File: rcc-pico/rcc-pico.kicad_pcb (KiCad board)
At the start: 2 copper layers, 78.7 x 59.5 mm, 24 parts, among them J1 PJ-006A, J2 Conn_01x03_Female, SW1 SW_Push, U1 AP63300WU-7, U2 PicoW, U3 Conn_03x20, U4 Conn_03x20

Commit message: finished schematic
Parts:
- removed C5-1, C5-2: 22μ, Capacitor_SMD:C_1210_3225Metric_Pad1.33x2.70mm_HandSolder
- added C1-1: 22μ, Capacitor_SMD:C_1210_3225Metric_Pad1.33x2.70mm_HandSolder, F.Cu at (118.2, 101.3)
- added C1-2: 22μ, Capacitor_SMD:C_1210_3225Metric_Pad1.33x2.70mm_HandSolder, F.Cu at (155.9, 66.0)
- added C5: 4.7u, Capacitor_SMD:C_0603_1608Metric_Pad1.08x0.95mm_HandSolder, F.Cu at (97.1, 110.8)
- added C6: 4.7u, Capacitor_SMD:C_0603_1608Metric_Pad1.08x0.95mm_HandSolder, F.Cu at (101.5, 110.8)
- added J10: Conn_3x3_female, Connector_PinHeader_2.54mm:PinHeader3x3_P2.54mm_Vertical, F.Cu at (155.5, 58.9)
- added J3: Conn_02x03_Top_Bottom, Connector_PinHeader_2.54mm:PinHeader_2x03_P2.54mm_Vertical, F.Cu at (126.9, 77.8)
- added J4: Conn_03x3_female, Connector_PinHeader_2.54mm:PinHeader3x3_P2.54mm_Vertical, F.Cu at (117.1, 98.4)
- added J5: Conn_03x9, 3rdparty:PinHeader_3x9_P2.54mm_Vertical, F.Cu at (116.8, 73.4)
- added J6: Conn_03x3_female, Connector_PinHeader_2.54mm:PinHeader3x3_P2.54mm_Vertical, F.Cu at (138.9, 85.4)
- added J7: Conn_02x03_Top_Bottom, Connector_PinHeader_2.54mm:PinHeader_2x03_P2.54mm_Vertical, F.Cu at (148.0, 64.2)
- added J8: Conn_04x4, Connector_PinHeader_2.54mm:PinHeader4x4_P_2.54mm_Vertical, F.Cu at (128.0, 74.7)
- added J9: Conn_02x02_Top_Bottom, Connector_PinHeader_2.54mm:PinHeader_2x02_P2.54mm_Vertical, F.Cu at (170.1, 50.4)
- added Q1: BSS138, Package_TO_SOT_SMD:SOT-23, F.Cu at (153.0, 73.8)
- added Q2: BSS138, Package_TO_SOT_SMD:SOT-23, F.Cu at (130.6, 95.6)
- added Q3: BSS138, Package_TO_SOT_SMD:SOT-23, F.Cu at (148.1, 73.8)
- added R4: 10K, Resistor_SMD:R_0402_1005Metric, F.Cu at (122.7, 100.1)
- added R5: 500, Resistor_SMD:R_0603_1608Metric, F.Cu at (154.9, 69.4)
- added R6: 10K, Resistor_SMD:R_0402_1005Metric, F.Cu at (113.7, 100.1)
- added R7: 10K, Resistor_SMD:R_0402_1005Metric, F.Cu at (123.6, 97.6)
- added R8: 10K, Resistor_SMD:R_0402_1005Metric, F.Cu at (126.5, 97.6)
- added R9: 10K, Resistor_SMD:R_0402_1005Metric, F.Cu at (169.0, 56.3)
- added SW-on/off2: SW_SPST, 3rdparty:SW-T2-4E-B-A2-MA2, F.Cu at (124.5, 52.6)
- C3: value 100n -> 0.1μ
- J2: value Conn_01x03_Female -> Screw_Terminal; footprint Connector_PinHeader_2.54mm:PinHeader_1x03_P2.54mm_Vertical -> TerminalBlock_Phoenix:TerminalBlock_Phoenix_MPT-0,5-2-2.54_1x02_P2.54mm_Horizontal
- L1: value 6.8u -> 4.7u; footprint Inductor_SMD:L_Wuerth_HCI-1365 -> Inductor_SMD:SIDMP-SP0530
- R3: value 500 -> 10K; footprint Resistor_SMD:R_0603_1608Metric -> Resistor_SMD:R_0402_1005Metric
- U4: value Conn_03x20 -> AP2115M-3.3TRG1; footprint 3rdparty:PinHeader_3x20_P2.54mm_Vertical -> Package_SO:AP2115M-3.3TRG1
- moved J2 92.3 mm to (82.3, 107.1)
- moved D1 87.3 mm to (105.7, 110.8), turned to 0 degrees
- moved C3 85.7 mm to (92.0, 110.6), turned to 0 degrees
- moved H3 84.5 mm to (111.6, 104.8)
- moved R2 80.6 mm to (110.8, 110.1), turned to 0 degrees
- moved C4 78.1 mm to (115.7, 109.7)
- moved R3 77.4 mm to (116.7, 104.4), turned to 0 degrees
- moved L1 70.5 mm to (103.4, 105.3)
- moved SW1 68.6 mm to (90.7, 102.8), turned to 0 degrees
- moved C1 68.1 mm to (125.2, 94.5), turned to 0 degrees
- moved J1 53.9 mm to (119.5, 78.1), turned to 0 degrees
- moved H1 43.2 mm to (164.2, 51.7)
- moved H2 38.3 mm to (135.4, 89.8)
- moved TP1 32.6 mm to (161.2, 62.1)
- moved SW-on/off1 31.9 mm to (138.8, 52.6)
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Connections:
- D1 pad 2: +5V -> +3.3V
- H1 pad 1: unconnected-(H1-Pad1) -> GND
- H2 pad 1: unconnected-(H2-Pad1) -> GND
- H3 pad 1: unconnected-(H3-Pad1) -> GND
- H4 pad 1: unconnected-(H4-Pad1) -> GND
- J2 pad 1: +9V -> /MTRPWR
- R3 pad 1: Net-(D1-Pad1) -> +5V
- R3 pad 2: GND -> /5V_PWM_1
- U2 pad 33: /AGND -> GND
- U2 pad 35: /ADC_VREF -> unconnected-(U2-Pad35)
- U2 pad 36: /3V3 -> unconnected-(U2-Pad36)
- U2 pad 37: /3V3_EN -> unconnected-(U2-Pad37)
- U2 pad 40: /VBUS -> unconnected-(U2-Pad40)
- U3 pad 1: GND -> /GPIO0
- U3 pad 10: GND -> /GPIO7
- U3 pad 11: GND -> /GPIO8
- U3 pad 12: GND -> /GPIO9
- U3 pad 14: GND -> /GPIO10
- U3 pad 15: GND -> /GPIO11
- U3 pad 16: GND -> /GPIO12
- U3 pad 17: GND -> /GPIO13
- U3 pad 19: GND -> /GPIO14
- U3 pad 2: GND -> /GPIO1
- U3 pad 20: GND -> /GPIO15
- U3 pad 21: +5V -> +3.3V
- U3 pad 22: +5V -> +3.3V
- U3 pad 23: +5V -> +3.3V
- U3 pad 24: +5V -> +3.3V
- U3 pad 25: +5V -> +3.3V
- U3 pad 26: +5V -> +3.3V
- U3 pad 27: +5V -> +3.3V
- U3 pad 28: +5V -> +3.3V
- U3 pad 29: +5V -> +3.3V
- U3 pad 30: +5V -> +3.3V
- U3 pad 31: +5V -> +3.3V
- U3 pad 32: +5V -> +3.3V
- U3 pad 33: +5V -> +3.3V
- U3 pad 34: +5V -> +3.3V
- U3 pad 35: +5V -> +3.3V
- U3 pad 36: +5V -> +3.3V
- U3 pad 37: +5V -> +3.3V
- U3 pad 38: +5V -> +3.3V
- U3 pad 39: +5V -> +3.3V
- U3 pad 4: GND -> /GPIO2
- U3 pad 40: +5V -> +3.3V
- U3 pad 41: /GPIO0 -> GND
- U3 pad 42: /GPIO1 -> GND
- U3 pad 44: /GPIO2 -> GND
- U3 pad 45: /GPIO3 -> GND
- U3 pad 46: /GPIO4 -> GND
- U3 pad 47: /GPIO5 -> GND
- U3 pad 49: /GPIO6 -> GND
- U3 pad 5: GND -> /GPIO3
- U3 pad 50: /GPIO7 -> GND
- U3 pad 51: /GPIO8 -> GND
- U3 pad 52: /GPIO9 -> GND
- U3 pad 54: /GPIO10 -> GND
- U3 pad 55: /GPIO11 -> GND
- U3 pad 56: /GPIO12 -> GND
- U3 pad 57: /GPIO13 -> GND
- U3 pad 59: /GPIO14 -> GND
- U3 pad 6: GND -> /GPIO4
- U3 pad 60: /GPIO15 -> GND
- U3 pad 7: GND -> /GPIO5
- U3 pad 9: GND -> /GPIO6
- U4 pad 1: /VBUS -> +3.3V
- U4 pad 2: +5V -> unconnected-(U4-Pad2)
- U4 pad 3: GND -> unconnected-(U4-Pad3)
- U4 pad 4: /3V3_EN -> unconnected-(U4-Pad4)
- U4 pad 5: /3V3 -> +5V
- U4 pad 6: /ADC_VREF -> GND
- U4 pad 7: /GPIO28 -> GND
- U4 pad 8: /AGND -> +5V
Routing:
- net +5V: track 227.8 -> 0.00 mm, vias 1 -> 0
- net +9V: track 45.0 -> 0.00 mm, vias 2 -> 0
- net /run: track 24.1 -> 0.00 mm
- net Net-(C3-Pad2): track 19.3 -> 0.00 mm
- net Net-(J1-Pad1): track 16.9 -> 0.00 mm
- net Net-(C4-Pad1): track 11.9 -> 0.00 mm
- net /GPIO18: track 7.29 -> 0.00 mm
- net /GPIO22: track 7.29 -> 0.00 mm
- net /ADC_VREF: track 7.29 -> 0.00 mm
- net /3V3_EN: track 7.29 -> 0.00 mm
- net /3V3: track 7.29 -> 0.00 mm
- net /VBUS: track 7.29 -> 0.00 mm
- net /GPIO28: track 7.29 -> 0.00 mm
- net /GPIO27: track 7.29 -> 0.00 mm
- net /GPIO26: track 7.29 -> 0.00 mm
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- removed copper zone on F.Cu, net GND
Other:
- board outline removed
- board text removed: "+5V"
- board text removed: "+9V BATTERY"
- board text removed: "+9V GND +5V"
- board text removed: "0 1"
- board text removed: "10 11 12 13"
- board text removed: "14 15"
- board text removed: "17 16"
- board text removed: "2 3 4 5"
- board text removed: "21 20 19 18"
- board text removed: "22"
- board text removed: "27 26"
- board text removed: "28"
- board text removed: "3V3 ADC_VREF"
- board text removed: "3V3_EN"
- board text removed: "6 7 8 9"
- board text removed: "AGND"
- board text removed: "GND"
- board text removed: "Jeannette Circe & Michael Giglia"
- board text removed: "L298N"
- board text removed: "ON OFF OFF"
- board text removed: "PICO"
- board text removed: "PICO RESET"
- board text removed: "Power Switch"
- board text removed: "ROBOTICS CRASH COURSE '23 RP PICO SHIELD v0.1"
- board text removed: "SUMMER STEM"
- board text removed: "THE COOPER UNION"
- board text removed: "USB"
- board text removed: "VBUS +5V GND"
- board text removed: "run"

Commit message: finished schematic and layout
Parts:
- removed C1-1, C1-2: 22μ, Capacitor_SMD:C_1210_3225Metric_Pad1.33x2.70mm_HandSolder
- removed J10: Conn_3x3_female, Connector_PinHeader_2.54mm:PinHeader3x3_P2.54mm_Vertical
- removed U3: Conn_03x20, 3rdparty:PinHeader_3x20_P2.54mm_Vertical
- added C7: 4.7u, Capacitor_SMD:C_0402_1005Metric, F.Cu at (87.1, 121.2)
- added C8: 4.7u, Capacitor_SMD:C_0402_1005Metric, F.Cu at (85.8, 130.1)
- C1, C2: footprint Capacitor_SMD:C_1210_3225Metric_Pad1.33x2.70mm_HandSolder -> Capacitor_SMD:C_0805_2012Metric
- C3: footprint Capacitor_SMD:C_1206_3216Metric_Pad1.33x1.80mm_HandSolder -> Capacitor_SMD:C_0402_1005Metric
- C4: footprint Capacitor_SMD:C_0603_1608Metric_Pad1.08x0.95mm_HandSolder -> Capacitor_SMD:C_0603_1608Metric
- C5, C6: value 4.7u -> 22μ; footprint Capacitor_SMD:C_0603_1608Metric_Pad1.08x0.95mm_HandSolder -> Capacitor_SMD:C_0805_2012Metric
- J2: footprint TerminalBlock_Phoenix:TerminalBlock_Phoenix_MPT-0,5-2-2.54_1x02_P2.54mm_Horizontal -> TerminalBlock:TCxx03_5mm_2x1
- J3: value Conn_02x03_Top_Bottom -> Conn_03x3_female; footprint Connector_PinHeader_2.54mm:PinHeader_2x03_P2.54mm_Vertical -> Connector_PinHeader_2.54mm:PinHeader3x3_P2.54mm_Vertical
- J4: value Conn_03x3_female -> Conn_3x4_female; footprint Connector_PinHeader_2.54mm:PinHeader3x3_P2.54mm_Vertical -> 3rdparty:PinHeader_3x4_P2.54mm_vertical
- J5: value Conn_03x9 -> Conn_03x10; footprint 3rdparty:PinHeader_3x9_P2.54mm_Vertical -> 3rdparty:PinHeader_3x11_P2.54mm_Vertical
- J6: value Conn_03x3_female -> Conn_02x04_Top_Bottom; footprint Connector_PinHeader_2.54mm:PinHeader3x3_P2.54mm_Vertical -> Connector_PinHeader_2.54mm:PinHeader_2x04_P2.54mm_Vertical
- J7: value Conn_02x03_Top_Bottom -> Conn_04x4; footprint Connector_PinHeader_2.54mm:PinHeader_2x03_P2.54mm_Vertical -> Connector_PinHeader_2.54mm:PinHeader4x4_P_2.54mm_Vertical
- J8: value Conn_04x4 -> Conn_3x3_female; footprint Connector_PinHeader_2.54mm:PinHeader4x4_P_2.54mm_Vertical -> Connector_PinHeader_2.54mm:PinHeader3x3_P2.54mm_Vertical
- J9: value Conn_02x02_Top_Bottom -> Conn_03x9; footprint Connector_PinHeader_2.54mm:PinHeader_2x02_P2.54mm_Vertical -> 3rdparty:PinHeader3x7+3
- L1: footprint Inductor_SMD:SIDMP-SP0530 -> Inductor_SMD:BWVS00606045
- R1: footprint Resistor_SMD:R_0805_2012Metric_Pad1.20x1.40mm_HandSolder -> Resistor_SMD:R_0402_1005Metric
- R2: footprint Resistor_SMD:R_1206_3216Metric -> Resistor_SMD:R_0402_1005Metric
- R3: value 10K -> 470
- R5: value 500 -> 10K; footprint Resistor_SMD:R_0603_1608Metric -> Resistor_SMD:R_0402_1005Metric
- SW-on/off1, SW-on/off2: footprint 3rdparty:SW-T2-4E-B-A2-MA2 -> 3rdparty:SW-T3-2B-A-A3-S1
- U1: footprint Package_TO_SOT_SMD:TSOT-23-6_HandSoldering -> Package_TO_SOT_SMD:TSOT-23-6
- U2: value PicoW -> AP2115M-3.3TRG1; footprint 3rdparty:RPi_Pico_SMD_TH -> Package_SO:AP2115M-3.3TRG1
- U4: value AP2115M-3.3TRG1 -> PicoW; footprint Package_SO:AP2115M-3.3TRG1 -> 3rdparty:RPi_Pico_SMD_TH
- moved J9 108.4 mm to (90.9, 124.4), turned to -90 degrees
- moved U1 103.8 mm to (98.2, 137.8), turned to 180 degrees
- moved C2 92.5 mm to (99.3, 134.9), turned to 180 degrees
- moved R9 92.3 mm to (95.7, 112.5), turned to -90 degrees
- moved SW-on/off1 84.8 mm to (135.0, 137.4), turned to -90 degrees
- moved SW-on/off2 78.2 mm to (122.7, 130.8), turned to 180 degrees
- moved R1 76.8 mm to (101.0, 139.5), turned to -90 degrees
- moved J7 68.5 mm to (92.2, 103.9), turned to 90 degrees
- moved Q3 63.5 mm to (98.2, 113.0), turned to 180 degrees
- moved R5 63.1 mm to (109.0, 112.8), turned to -90 degrees
- moved TP1 62.7 mm to (142.6, 122.0), turned to 90 degrees
- moved H4 59.5 mm to (79.7, 123.2)
- moved J1 58.0 mm to (138.8, 132.8), turned to 180 degrees
- moved Q1 57.2 mm to (111.6, 113.3), turned to 180 degrees
- moved U2 53.2 mm to (85.8, 125.7), turned to -90 degrees
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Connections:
- C5 pad 1: +3.3V -> +5V
- J3 pad 1: /GPIO11 -> GND
- J3 pad 2: /3V3_PWM_1 -> GND
- J3 pad 3: /GPIO12 -> GND
- J3 pad 4: /3V3_PWM_2 -> +5V
- J3 pad 5: /GPIO13 -> +5V
- J3 pad 6: /3V3_PWM_3 -> +5V
- J4 pad 1: GND -> /GPIO0
- J4 pad 2: GND -> /GPIO1
- J4 pad 3: GND -> /GPIO2
- J4 pad 4: +5V -> /GPIO3
- J4 pad 5: +5V -> +3.3V
- J4 pad 6: +5V -> +3.3V
- J4 pad 7: /5V_PWM_1 -> +3.3V
- J4 pad 8: /5V_PWM_2 -> +3.3V
- J4 pad 9: /5V_PWM_3 -> GND
- J5 pad 1: GND -> /GPIO4
- J5 pad 10: +3.3V -> /GPIO13
- J5 pad 19: /GPIO22 -> +3.3V
- J5 pad 2: GND -> /GPIO5
- J5 pad 20: GND -> +3.3V
- J5 pad 21: /GPIO21 -> GND
- J5 pad 22: /GPIO20 -> GND
- J5 pad 23: /GPIO19 -> GND
- J5 pad 24: /GPIO18 -> GND
- J5 pad 26: /GPIO17 -> GND
- J5 pad 27: /GPIO16 -> GND
- J5 pad 3: GND -> /GPIO6
- J5 pad 4: GND -> /GPIO7
- J5 pad 5: GND -> /GPIO8
- J5 pad 6: GND -> /GPIO9
- J5 pad 7: GND -> /GPIO10
- J5 pad 8: GND -> /GPIO11
- J5 pad 9: GND -> /GPIO12
- J6 pad 1: +3.3V -> /SCL
- J6 pad 2: +3.3V -> /SDA
- J6 pad 3: +3.3V -> /GPIO15
- J6 pad 4: /ADC0 -> /GPIO14
- J6 pad 5: /ADC1 -> +3.3V
- J6 pad 6: /ADC2 -> +3.3V
- J7 pad 1: /GPIO28 -> +3.3V
- J7 pad 2: /ADC0 -> +3.3V
- J7 pad 3: /GPIO27 -> +3.3V
- J7 pad 4: /ADC1 -> +3.3V
- J7 pad 5: /GPIO26 -> GND
- J7 pad 6: /ADC2 -> GND
- J8 pad 1: +3.3V -> GND
- J8 pad 2: +3.3V -> GND
- J8 pad 3: +3.3V -> GND
- J8 pad 5: GND -> +3.3V
- J8 pad 6: GND -> +3.3V
- J8 pad 7: GND -> /GPIO28
- J8 pad 8: GND -> /GPIO27
- J8 pad 9: /SCL -> /GPIO26
- J9 pad 1: /GPIO14 -> GND
- J9 pad 2: /SDA -> GND
- J9 pad 3: /GPIO15 -> GND
- J9 pad 4: /SCL -> GND
- R3 pad 1: +5V -> Net-(D1-Pad1)
- R3 pad 2: /5V_PWM_1 -> GND
- R4 pad 1: +3.3V -> +5V
- R4 pad 2: /3V3_PWM_1 -> /5V_PWM_1
- R5 pad 1: Net-(D1-Pad1) -> +3.3V
- R5 pad 2: GND -> /3V3_PWM_1
- U2 pad 1: /GPIO0 -> +3.3V
- U2 pad 2: /GPIO1 -> unconnected-(U2-Pad2)
- U2 pad 3: GND -> unconnected-(U2-Pad3)
- U2 pad 4: /GPIO2 -> unconnected-(U2-Pad4)
- U2 pad 5: /GPIO3 -> +5V
- U2 pad 6: /GPIO4 -> GND
- U2 pad 7: /GPIO5 -> GND
- U2 pad 8: GND -> +5V
- U4 pad 1: +3.3V -> /GPIO0
- U4 pad 2: unconnected-(U4-Pad2) -> /GPIO1
- U4 pad 3: unconnected-(U4-Pad3) -> GND
- U4 pad 4: unconnected-(U4-Pad4) -> /GPIO2
- U4 pad 5: +5V -> /GPIO3
- U4 pad 6: GND -> /GPIO4
- U4 pad 7: GND -> /GPIO5
- U4 pad 8: +5V -> GND
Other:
- board outline added: 70.6 x 55.2 mm
- board text added: "+5V"
- board text added: "+9V"
- board text added: "0"
- board text added: "1"
- board text added: "10"
- board text added: "11"
- board text added: "12"
- board text added: "13"
- board text added: "14"
- board text added: "15↑"
- board text added: "16"
- board text added: "17"
- board text added: "18"
- board text added: "18↓17↓16↓"
- board text added: "19"
- board text added: "2"
- board text added: "20"
- board text added: "21"
- board text added: "22"
- board text added: "3"
- board text added: "3V3"
- board text added: "4"
- board text added: "5"
- board text added: "5V~PWM"
- board text added: "6"
- board text added: "7"
- board text added: "8"
- board text added: "9"
- board text added: "ADC0"
- board text added: "ADC1"
- board text added: "ADC2"
- board text added: "BATTERY"
- board text added: "CONNECT 14&15 TO USE I2C1 EXTENSION"
- board text added: "CONNECT TO USE 5V~PWM"
- board text added: "FRONT"
- board text added: "GND"
- board text added: "GND +9V"
- board text added: "GPIO"
- board text added: "I2C1"
- board text added: "L298N"
- board text added: "L298N PWR"
- board text added: "MOTOR ON→"
- board text added: "PICO ON→"
- board text added: "REAR"
- board text added: "RESET"
- board text added: "SCL"
- board text added: "SDA"
- board text added: "↓"

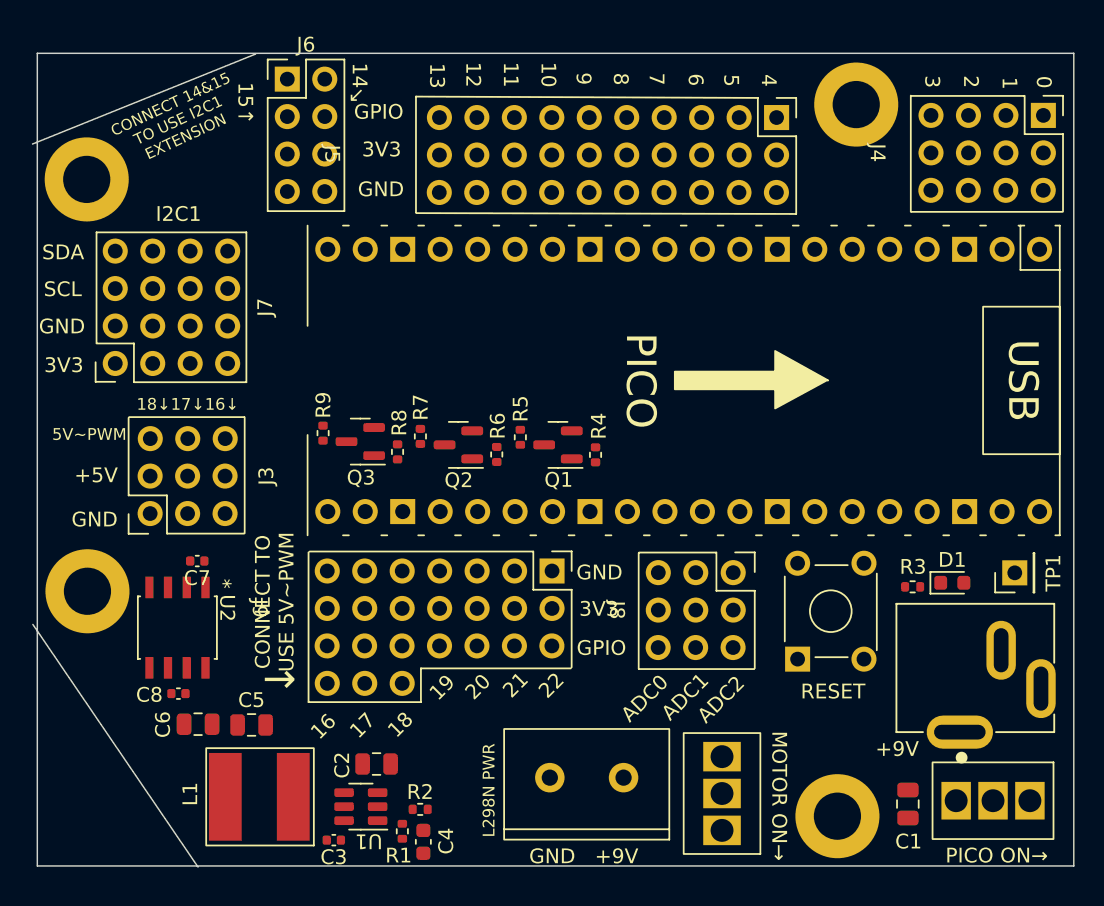
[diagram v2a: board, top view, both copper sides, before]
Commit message: first layout of traces
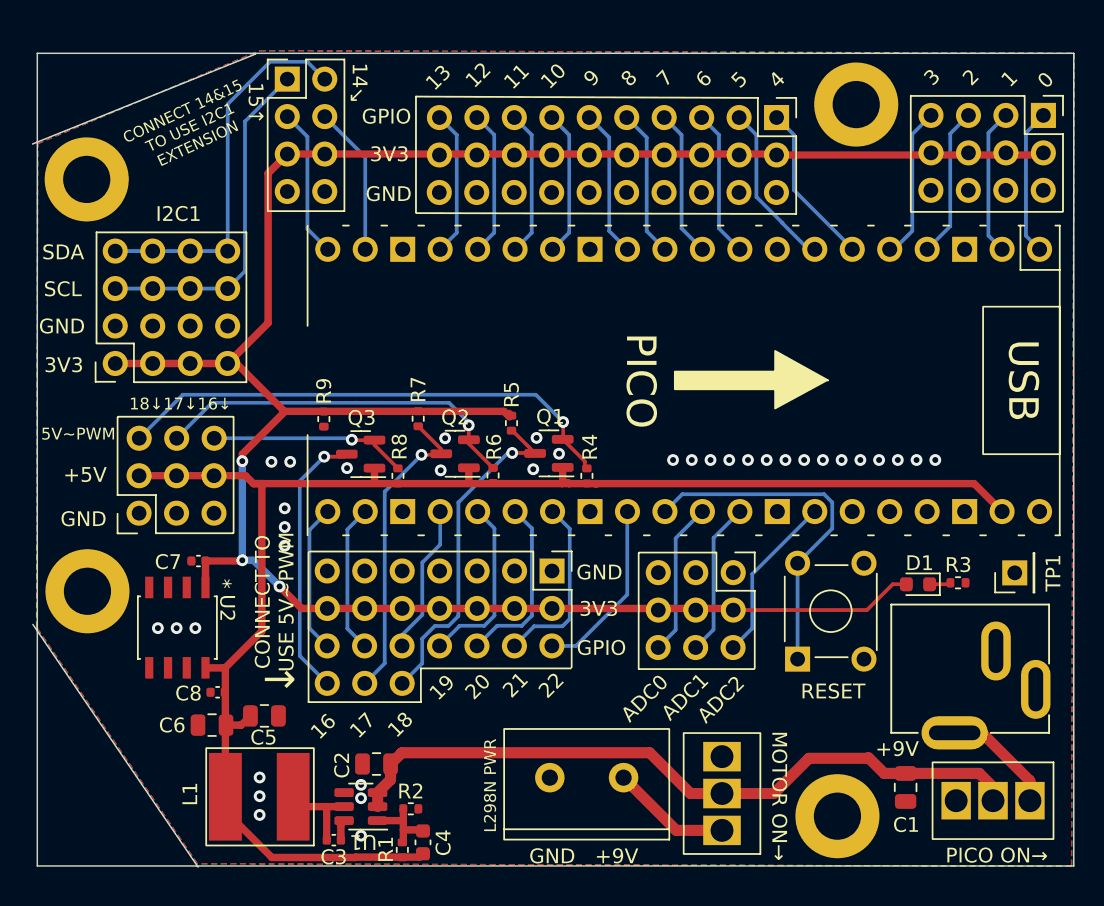
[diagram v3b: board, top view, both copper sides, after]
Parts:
- moved R3 3.09 mm to (138.7, 122.6), turned to 0 degrees
- moved C8 2.66 mm to (88.5, 130.1)
- moved D1 2.33 mm to (136.0, 122.7), turned to 180 degrees
- moved R8 1.63 mm to (100.7, 115.4)
- moved R4 1.54 mm to (113.5, 115.4)
- moved R6 1.45 mm to (107.2, 115.3)
- moved R1 1.26 mm to (101.0, 140.7)
- moved R7 1.21 mm to (102.1, 111.5)
- moved C1 1.13 mm to (135.2, 136.5)
- moved R5 1.13 mm to (108.4, 111.8)
- moved C5 1.07 mm to (91.7, 131.7)
- moved C6 0.95 mm to (88.1, 132.3)
- moved R9 0.95 mm to (95.7, 111.5)
- moved Q3 0.85 mm to (98.2, 113.9)
- moved Q1 0.84 mm to (111.0, 113.8)
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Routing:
- net +3.3V: track 0.00 -> 158.3 mm, vias 0 -> 3
- net +5V: track 0.00 -> 103.5 mm
- net +9V: track 0.00 -> 48.3 mm
- net /5V_PWM_1: track 0.00 -> 34.2 mm, vias 0 -> 1
- net /SDA: track 0.00 -> 25.8 mm
- net /5V_PWM_2: track 0.00 -> 25.1 mm, vias 0 -> 1
- net /run: track 0.00 -> 23.7 mm
- net /3V3_PWM_1: track 0.00 -> 23.6 mm, vias 0 -> 1
- net /SCL: track 0.00 -> 23.5 mm
- net /3V3_PWM_2: track 0.00 -> 21.0 mm, vias 0 -> 1
- net /3V3_PWM_3: track 0.00 -> 18.6 mm, vias 0 -> 1
- net /5V_PWM_3: track 0.00 -> 13.5 mm, vias 0 -> 1
- net /GPIO21: track 0.00 -> 12.3 mm
- net /GPIO22: track 0.00 -> 12.2 mm
- net /GPIO20: track 0.00 -> 12.1 mm
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- added copper zone on B.Cu, net GND
- added copper zone on F.Cu, net GND

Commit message: ordered JLC
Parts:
- added C9: 0.1μ, Capacitor_SMD:C_0402_1005Metric, F.Cu at (140.4, 115.5)
- added J10: Conn_02x04_Top_Bottom, Connector_PinHeader_2.54mm:PinHeader_2x04_P2.54mm_Vertical-down, F.Cu at (83.5, 112.0)
- J7: value Conn_04x4 -> Conn_02x04_Top_Bottom; footprint Connector_PinHeader_2.54mm:PinHeader4x4_P_2.54mm_Vertical -> Connector_PinHeader_2.54mm:PinHeader_2x04_P2.54mm_Vertical-down
- moved J7 8.40 mm to (89.7, 112.0), turned to 0 degrees
- moved R4 1.11 mm to (113.5, 114.3)
- moved R6 1.05 mm to (107.1, 114.3)
- moved R8 1.04 mm to (100.8, 114.3)
- moved R9 1.00 mm to (95.7, 112.5)
- moved C8 0.89 mm to (87.7, 130.3), turned to -90 degrees
- moved R7 0.78 mm to (102.1, 112.3)
- moved C5 0.78 mm to (91.7, 132.4)
- moved J6 0.59 mm to (93.8, 88.3)
- moved R5 0.58 mm to (108.5, 112.4)
- moved J5 0.35 mm to (95.8, 93.2)
- moved C2 0.24 mm to (99.2, 134.7)
- moved J4 0.24 mm to (132.6, 93.3)
- moved R1 0.19 mm to (101.0, 140.6)
- moved R2 0.18 mm to (101.6, 138.1)
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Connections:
- J7 pad 1: +3.3V -> /SDA
- J7 pad 2: +3.3V -> /SCL
- J7 pad 3: +3.3V -> GND
- J7 pad 5: GND -> /SDA
- J7 pad 6: GND -> /SCL
- J7 pad 8: GND -> +3.3V
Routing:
- net +5V: track 103.5 -> 114.9 mm
- net +3.3V: track 158.3 -> 160.7 mm
- net /SDA: track 25.8 -> 27.2 mm
- net /SCL: track 23.5 -> 24.9 mm
- net /3V3_PWM_2: track 21.0 -> 19.7 mm
- net /3V3_PWM_1: track 23.6 -> 22.4 mm
- net /3V3_PWM_3: track 18.6 -> 19.7 mm
- net /5V_PWM_2: track 25.1 -> 24.4 mm
- net /5V_PWM_3: track 13.5 -> 12.9 mm
- net GND: vias 35 -> 48
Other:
- board size 70.6 x 55.2 mm -> 70 x 55.6 mm
- board text added: "15"
- board text added: "26,27,28"
- board text added: "CONNECT TO USE I2C1 EXTENSION"
- board text added: "RP PICO (AS A SHIELD) v0.1 JEANNETTE CIRCE CATHERINE VAN WEST MICHAEL GIGLIA APRIL 2023"
- board text added: "split this block"
- board text removed: "15↑"
- board text removed: "CONNECT 14&15 TO USE I2C1 EXTENSION"
